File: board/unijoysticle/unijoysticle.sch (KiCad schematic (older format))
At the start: 12 parts, among them IC1 7405, IC2 7405, J1 DB9_Female, J2 DB9_Female, J3 Barrel_Jack, SW1 SW_Push

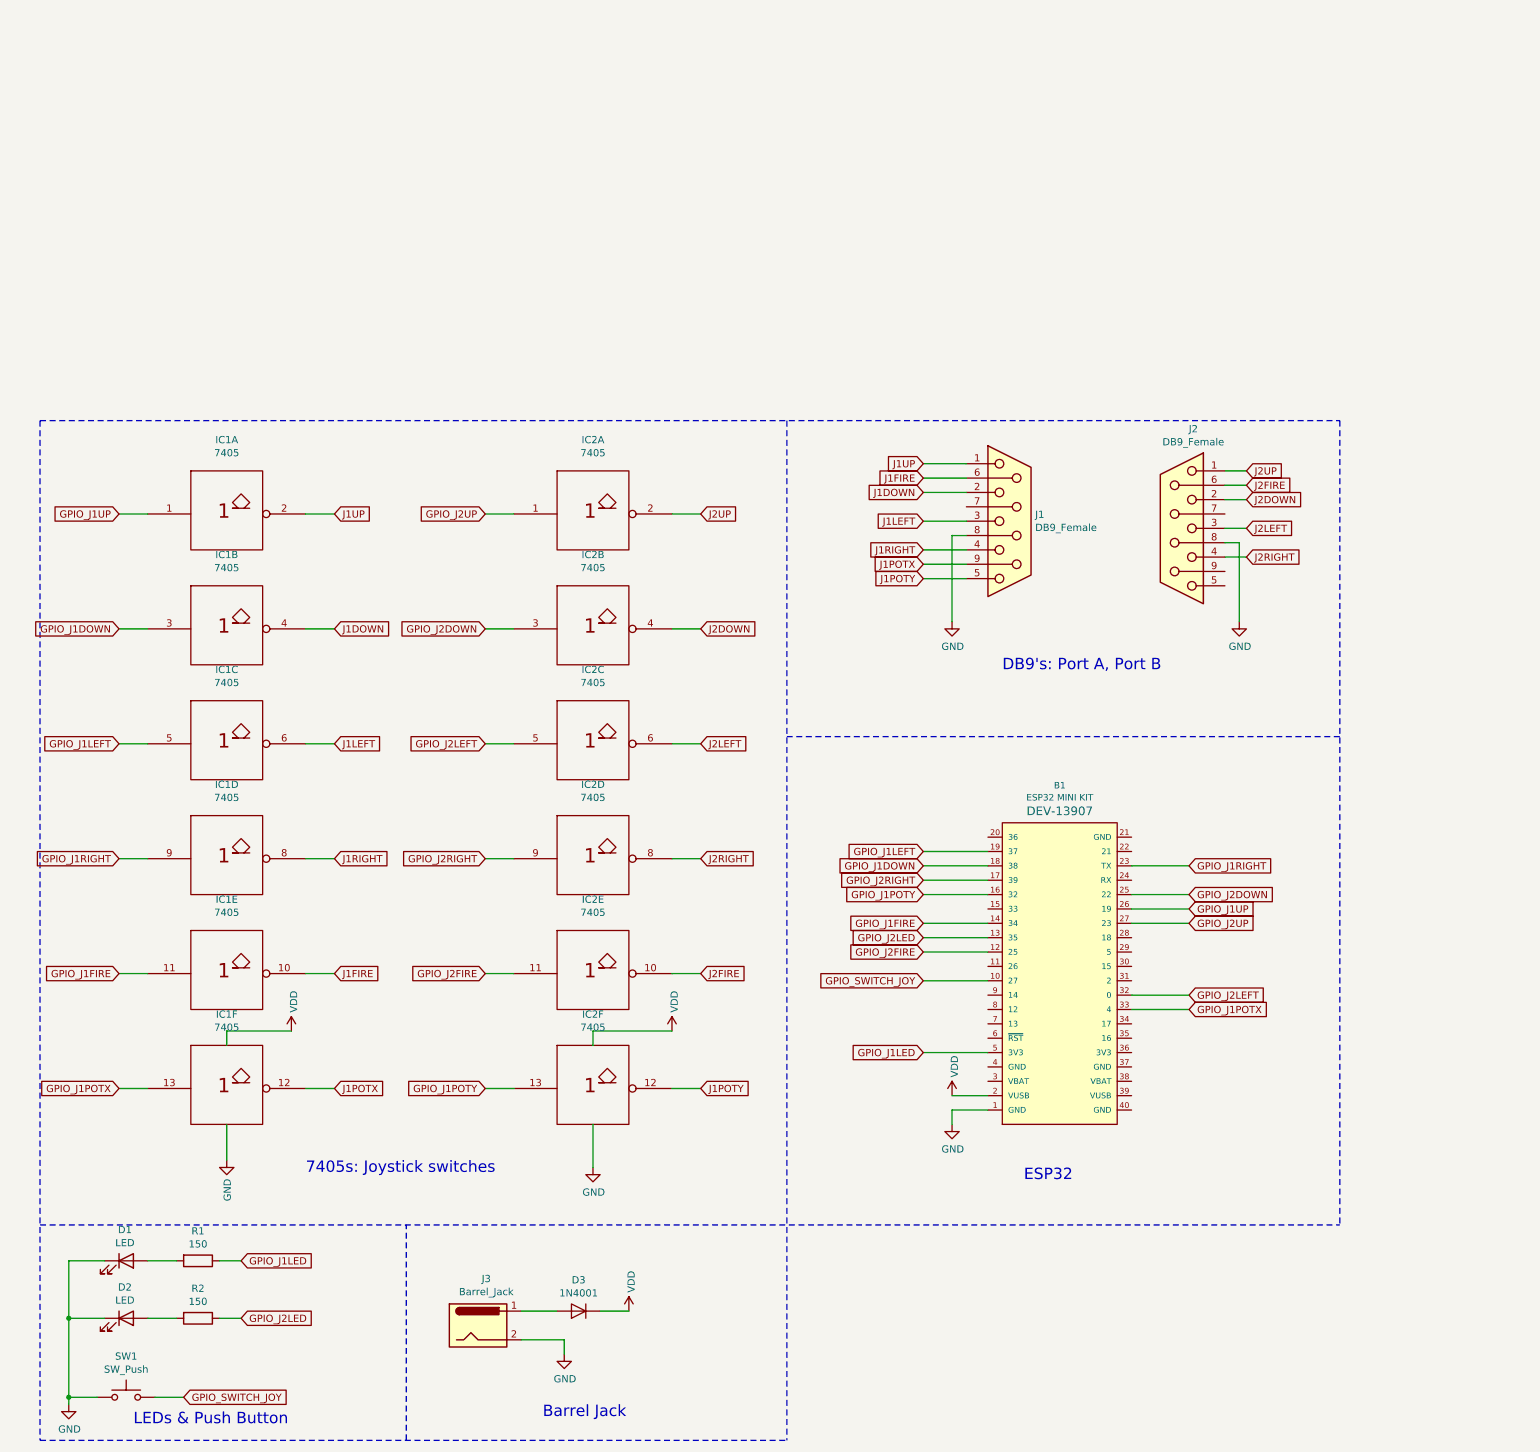
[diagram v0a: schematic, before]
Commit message: schematic: support for power from c64
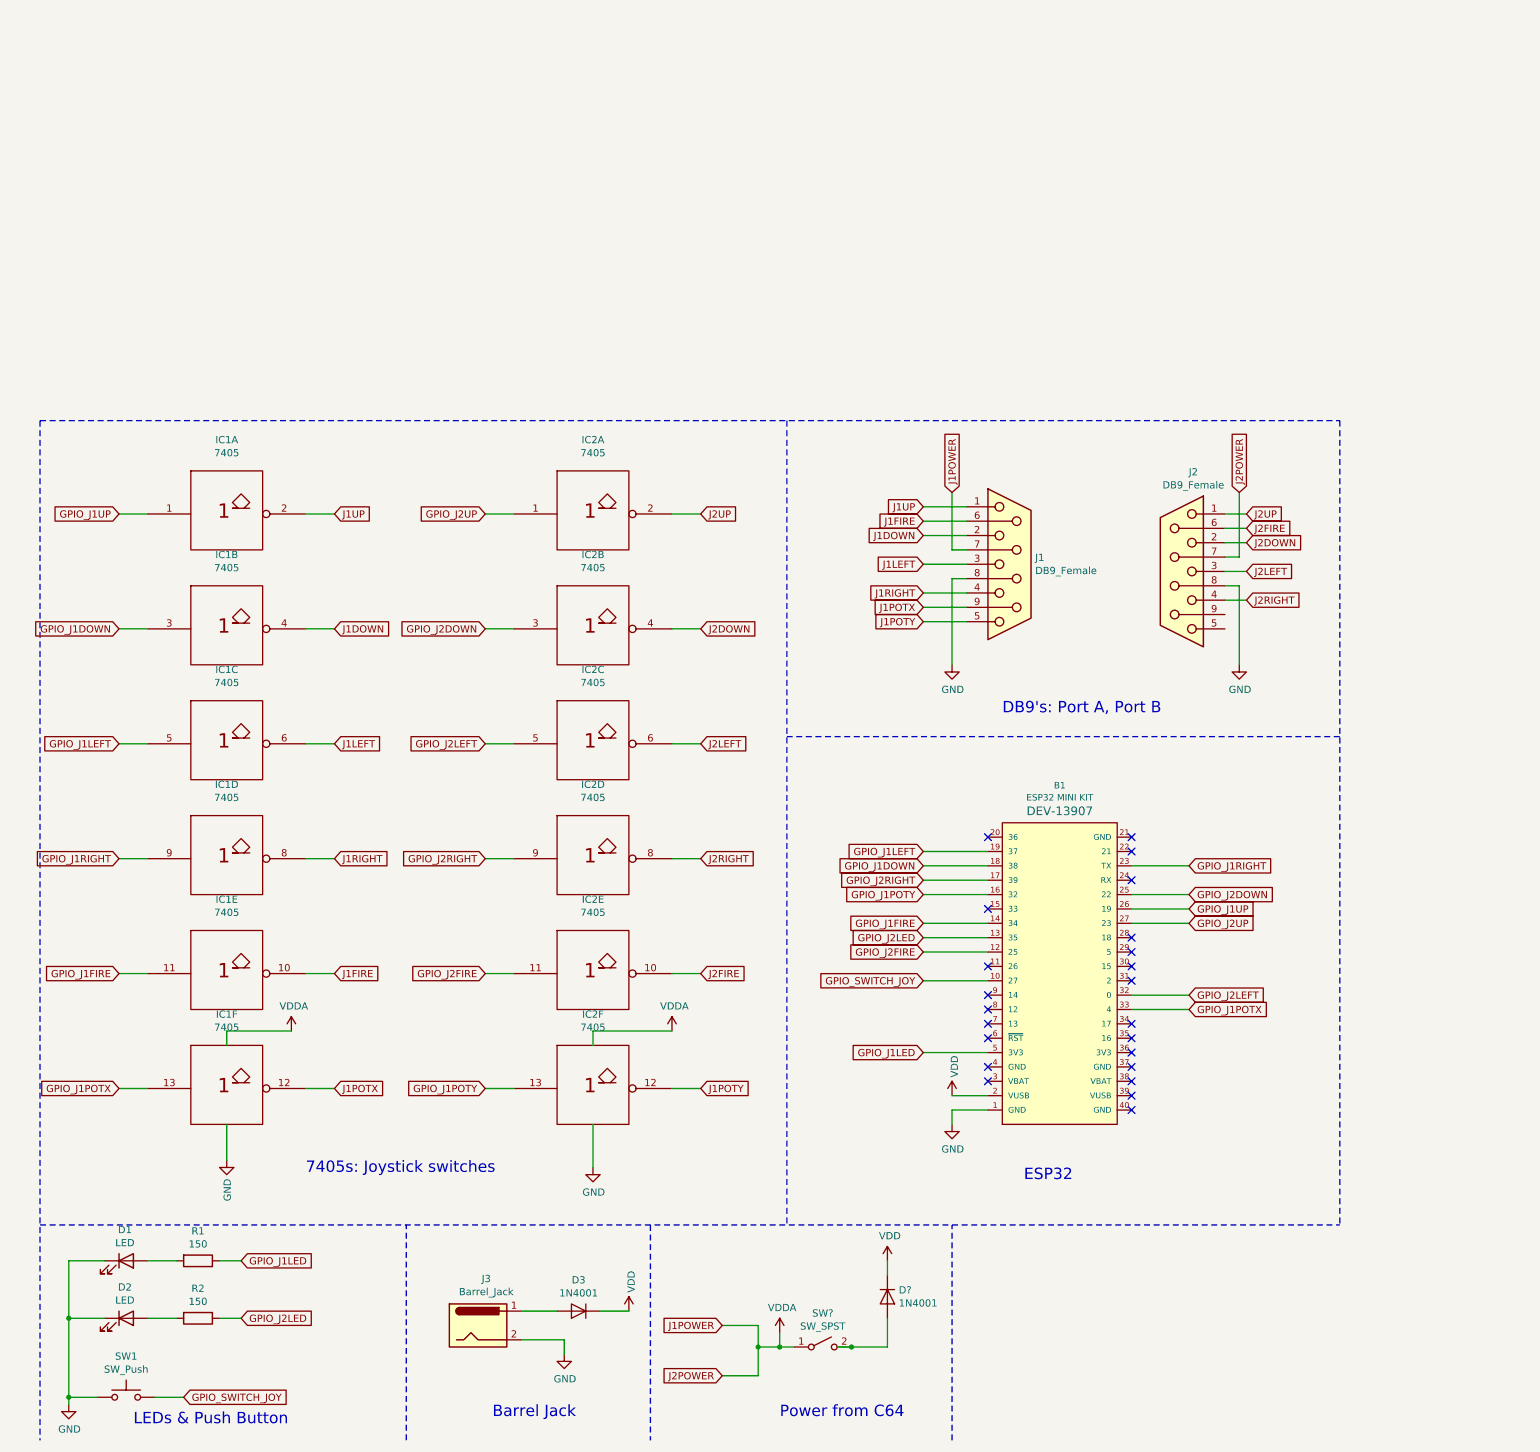
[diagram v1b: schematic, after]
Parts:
- added D?: 1N4001, Diode_THT:D_DO-41_SOD81_P10.16mm_Horizontal, symbol Diode:1N4001
- added SW?: SW_SPST, symbol Switch:SW_SPST
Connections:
- net VDD: now also D?.1 (K); no longer IC1.14 (Vcc), IC2.14 (Vcc)
- net VDDA: now reaches J1.7
- net VDDA: now also IC1.14 (Vcc), IC2.14 (Vcc), J2.7, SW?.1 (A)
- new net: D?.2 (A), SW?.2 (B)
- no-connect marks 0 -> 23
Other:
- note added: "Power from C64"
- moved on the sheet: J1, J2
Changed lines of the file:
@@
 EESchema Schematic File Version 4
 LIBS:unijoysticle-cache
-EELAYER 29 0
+EELAYER 30 0
 EELAYER END
 $Descr A4 11693 8268
@@
 Sheet 1 1
 Title "Unijoysticle 2"
-Date "2019-03-28"
-Rev "B"
+Date "2019-09-21"
+Rev "C"
 Comp "Retro Moe"
 Comment1 "Ricardo Quesada"
@@
 GPIO_J1POTY
 Wire Wire Line
-	7000 1000 6700 1000
-Wire Wire Line
-	7000 1100 6700 1100
-Wire Wire Line
-	7000 1200 6700 1200
+	7000 1300 6700 1300
 Wire Wire Line
 	7000 1400 6700 1400
 Wire Wire Line
-	7000 1600 6700 1600
+	7000 1500 6700 1500
 Wire Wire Line
 	7000 1700 6700 1700
 Wire Wire Line
-	7000 1800 6700 1800
-Text GLabel 6700 1000 0    50   Input ~ 0
+	7000 1900 6700 1900
+Wire Wire Line
+	7000 2000 6700 2000
+Wire Wire Line
+	7000 2100 6700 2100
+Text GLabel 6700 1300 0    50   Input ~ 0
 J1UP
-Text GLabel 6700 1200 0    50   Input ~ 0
+Text GLabel 6700 1500 0    50   Input ~ 0
 J1DOWN
+Text GLabel 6700 1700 0    50   Input ~ 0
+J1LEFT
 Text GLabel 6700 1400 0    50   Input ~ 0
-J1LEFT
-Text GLabel 6700 1100 0    50   Input ~ 0
 J1FIRE
-Text GLabel 6700 1800 0    50   Input ~ 0
+Text GLabel 6700 2100 0    50   Input ~ 0
 J1POTY
-Text GLabel 6700 1700 0    50   Input ~ 0
+Text GLabel 6700 2000 0    50   Input ~ 0
 J1POTX
-Text GLabel 6700 1600 0    50   Input ~ 0
+Text GLabel 6700 1900 0    50   Input ~ 0
 J1RIGHT
-Text GLabel 8950 1050 2    50   Input ~ 0
+Text GLabel 8950 1350 2    50   Input ~ 0
 J2UP
-Text GLabel 8950 1250 2    50   Input ~ 0
+Text GLabel 8950 1550 2    50   Input ~ 0
 J2DOWN
+Text GLabel 8950 1750 2    50   Input ~ 0
+J2LEFT
+Text GLabel 8950 1950 2    50   Input ~ 0
+J2RIGHT
 Text GLabel 8950 1450 2    50   Input ~ 0
-J2LEFT
-Text GLabel 8950 1650 2    50   Input ~ 0
-J2RIGHT
-Text GLabel 8950 1150 2    50   Input ~ 0
 J2FIRE
 Text GLabel 5150 1350 2    50   Input ~ 0
@@
 L Connector:DB9_Female J1
 U 1 1 5C705949
-P 7300 1400
-F 0 "J1" H 7479 1446 50  0000 L CNN
-F 1 "DB9_Female" H 7479 1355 50  0000 L CNN
-F 2 "Connector_Dsub:DSUB-9_Female_Horizontal_P2.77x2.84mm_EdgePinOffset9.40mm" H 7300 1400 50  0001 C CNN
-F 3 "" H 7300 1400 50  0001 C CNN
-	1    7300 1400
+P 7300 1700
+F 0 "J1" H 7479 1746 50  0000 L CNN
+F 1 "DB9_Female" H 7479 1655 50  0000 L CNN
+F 2 "Connector_Dsub:DSUB-9_Female_Horizontal_P2.77x2.84mm_EdgePinOffset9.40mm" H 7300 1700 50  0001 C CNN
+F 3 "" H 7300 1700 50  0001 C CNN
+	1    7300 1700
 	1    0    0    -1
 $EndComp
@@
 L Connector:DB9_Female J2
 U 1 1 5C705C0F
-P 8500 1450
-F 0 "J2" H 8420 2142 50  0000 C CNN
-F 1 "DB9_Female" H 8420 2051 50  0000 C CNN
-F 2 "Connector_Dsub:DSUB-9_Female_Horizontal_P2.77x2.84mm_EdgePinOffset9.40mm" H 8500 1450 50  0001 C CNN
-F 3 "" H 8500 1450 50  0001 C CNN
-	1    8500 1450
+P 8500 1750
+F 0 "J2" H 8420 2442 50  0000 C CNN
+F 1 "DB9_Female" H 8420 2351 50  0000 C CNN
+F 2 "Connector_Dsub:DSUB-9_Female_Horizontal_P2.77x2.84mm_EdgePinOffset9.40mm" H 8500 1750 50  0001 C CNN
+F 3 "" H 8500 1750 50  0001 C CNN
+	1    8500 1750
 	-1   0    0    -1
 $EndComp
 Wire Wire Line
-	8800 1050 8950 1050
-Wire Wire Line
-	8800 1150 8950 1150
-Wire Wire Line
-	8800 1250 8950 1250
-Wire Wire Line
-	8950 1450 8800 1450
-Wire Wire Line
-	8950 1650 8800 1650
+	8800 1350 8950 1350
+Wire Wire Line
+	8800 1450 8950 1450
+Wire Wire Line
+	8800 1550 8950 1550
+Wire Wire Line
+	8950 1750 8800 1750
+Wire Wire Line
+	8950 1950 8800 1950
 Wire Wire Line
 	8150 4200 8550 4200
@@
 Wire Wire Line
 	1100 5350 1300 5350
-$Comp
-L power:VDD #PWR0105
-U 1 1 5C862F14
-P 2300 4950
-F 0 "#PWR0105" H 2300 4800 50  0001 C CNN
-F 1 "VDD" V 2317 5078 50  0000 L CNN
-F 2 "" H 2300 4950 50  0001 C CNN
-F 3 "" H 2300 4950 50  0001 C CNN
-	1    2300 4950
-	1    0    0    -1
-$EndComp
 Wire Wire Line
 	2300 4950 1850 4950
@@
 Wire Wire Line
 	4400 4950 4950 4950
-$Comp
-L power:VDD #PWR0106
-U 1 1 5C86D74A
-P 4950 4950
-F 0 "#PWR0106" H 4950 4800 50  0001 C CNN
-F 1 "VDD" V 4967 5078 50  0000 L CNN
-F 2 "" H 4950 4950 50  0001 C CNN
-F 3 "" H 4950 4950 50  0001 C CNN
-	1    4950 4950
-	1    0    0    -1
-$EndComp
 $Comp
 L Device:LED D1
@@
 	1800 6950 1950 6950
 Wire Wire Line
-	8800 1550 8900 1550
-Wire Wire Line
-	8900 1550 8900 2100
-Wire Wire Line
-	7000 1500 6900 1500
-Wire Wire Line
-	6900 1500 6900 2100
+	8800 1850 8900 1850
+Wire Wire Line
+	8900 1850 8900 2400
+Wire Wire Line
+	7000 1800 6900 1800
+Wire Wire Line
+	6900 1800 6900 2400
 $Comp
 L power:GND #PWR0102
 U 1 1 5C8CE940
-P 6900 2100
-F 0 "#PWR0102" H 6900 1850 50  0001 C CNN
-F 1 "GND" H 6905 1927 50  0000 C CNN
-F 2 "" H 6900 2100 50  0001 C CNN
-F 3 "" H 6900 2100 50  0001 C CNN
-	1    6900 2100
+P 6900 2400
+F 0 "#PWR0102" H 6900 2150 50  0001 C CNN
+F 1 "GND" H 6905 2227 50  0000 C CNN
+F 2 "" H 6900 2400 50  0001 C CNN
+F 3 "" H 6900 2400 50  0001 C CNN
+	1    6900 2400
 	1    0    0    -1
 $EndComp
@@
 L power:GND #PWR0108
 U 1 1 5C8CEFE9
-P 8900 2100
-F 0 "#PWR0108" H 8900 1850 50  0001 C CNN
-F 1 "GND" H 8905 1927 50  0000 C CNN
-F 2 "" H 8900 2100 50  0001 C CNN
-F 3 "" H 8900 2100 50  0001 C CNN
-	1    8900 2100
+P 8900 2400
+F 0 "#PWR0108" H 8900 2150 50  0001 C CNN
+F 1 "GND" H 8905 2227 50  0000 C CNN
+F 2 "" H 8900 2400 50  0001 C CNN
+F 3 "" H 8900 2400 50  0001 C CNN
+	1    8900 2400
 	1    0    0    -1
 $EndComp
@@
 Wire Notes Line
 	550  700  9600 700
-Text Notes 7250 2450 0    79   ~ 0
+Text Notes 7250 2750 0    79   ~ 0
 DB9's: Port A, Port B
 Wire Notes Line
@@
 Text Notes 1200 7700 0    79   ~ 0
 LEDs & Push Button
-Wire Notes Line
-	5750 700  5750 7800
-Wire Notes Line
-	550  7800 5750 7800
-Text Notes 4050 7650 0    79   ~ 0
+Text Notes 3700 7650 0    79   ~ 0
 Barrel Jack
 $Comp
@@
 	1    0    0    -1
 $EndComp
+Wire Wire Line
+	8800 1650 8900 1650
+Wire Wire Line
+	8900 1650 8900 1200
+Wire Wire Line
+	7000 1600 6900 1600
+Wire Wire Line
+	6900 1600 6900 1200
+$Comp
+L power:VDDA #PWR?
+U 1 1 5D8CE89E
+P 2300 4950
+F 0 "#PWR?" H 2300 4800 50  0001 C CNN
+F 1 "VDDA" H 2317 5123 50  0000 C CNN
+F 2 "" H 2300 4950 50  0001 C CNN
+F 3 "" H 2300 4950 50  0001 C CNN
+	1    2300 4950
+	1    0    0    -1
+$EndComp
+$Comp
+L power:VDDA #PWR?
+U 1 1 5D8CF370
+P 4950 4950
+F 0 "#PWR?" H 4950 4800 50  0001 C CNN
+F 1 "VDDA" H 4967 5123 50  0000 C CNN
+F 2 "" H 4950 4950 50  0001 C CNN
+F 3 "" H 4950 4950 50  0001 C CNN
+	1    4950 4950
+	1    0    0    -1
+$EndComp
+Text GLabel 6900 1200 1    50   Input ~ 0
+J1POWER
+Text GLabel 8900 1200 1    50   Input ~ 0
+J2POWER
+NoConn ~ 8150 5500
+NoConn ~ 8150 5400
+NoConn ~ 8150 5300
+NoConn ~ 8150 5200
+NoConn ~ 8150 5100
+NoConn ~ 8150 5000
+NoConn ~ 8150 4900
+NoConn ~ 8150 4600
+NoConn ~ 8150 4500
+NoConn ~ 8150 4400
+NoConn ~ 8150 4300
+NoConn ~ 8150 3900
+NoConn ~ 8150 3700
+NoConn ~ 8150 3600
+NoConn ~ 7150 3600
+NoConn ~ 7150 4100
+NoConn ~ 7150 4500
+NoConn ~ 7150 4700
+NoConn ~ 7150 4800
+NoConn ~ 7150 4900
+NoConn ~ 7150 5000
+NoConn ~ 7150 5200
+NoConn ~ 7150 5300
+Text GLabel 5300 7000 0    50   Input ~ 0
+J1POWER
+Text GLabel 5300 7350 0    50   Input ~ 0
+J2POWER
+Wire Wire Line
+	5300 7000 5550 7000
+Wire Wire Line
+	5550 7350 5300 7350
+Wire Wire Line
+	6100 7150 6200 7150
+$Comp
+L power:VDD #PWR?
+U 1 1 5D9B72D2
+P 6450 6550
+F 0 "#PWR?" H 6450 6400 50  0001 C CNN
+F 1 "VDD" H 6467 6723 50  0000 C CNN
+F 2 "" H 6450 6550 50  0001 C CNN
+F 3 "" H 6450 6550 50  0001 C CNN
+	1    6450 6550
+	1    0    0    -1
+$EndComp
+$Comp
+L Switch:SW_SPST SW?
+U 1 1 5D9BBF38
+P 6000 7150
+F 0 "SW?" H 6000 7385 50  0000 C CNN
+F 1 "SW_SPST" H 6000 7294 50  0000 C CNN
+F 2 "" H 6000 7150 50  0001 C CNN
+F 3 "~" H 6000 7150 50  0001 C CNN
+	1    6000 7150
+	1    0    0    -1
+$EndComp
+Wire Wire Line
+	5550 7000 5550 7150
+Wire Wire Line
+	5550 7150 5700 7150
+Connection ~ 5550 7150
+Wire Wire Line
+	5550 7150 5550 7350
+Wire Wire Line
+	5700 7150 5700 7050
+$Comp
+L power:VDDA #PWR?
+U 1 1 5D9F1571
+P 5700 7050
+F 0 "#PWR?" H 5700 6900 50  0001 C CNN
+F 1 "VDDA" H 5717 7223 50  0000 C CNN
+F 2 "" H 5700 7050 50  0001 C CNN
+F 3 "" H 5700 7050 50  0001 C CNN
+	1    5700 7050
+	1    0    0    -1
+$EndComp
+Wire Wire Line
+	5800 7150 5700 7150
+Connection ~ 5700 7150
+Wire Wire Line
+	6200 7150 6450 7150
+Wire Wire Line
+	6450 7150 6450 6950
+Connection ~ 6200 7150
+$Comp
+L Diode:1N4001 D?
+U 1 1 5DA3B4FA
+P 6450 6800
+F 0 "D?" V 6404 6879 50  0000 L CNN
+F 1 "1N4001" V 6495 6879 50  0000 L CNN
+F 2 "Diode_THT:D_DO-41_SOD81_P10.16mm_Horizontal" H 6450 6625 50  0001 C CNN
+F 3 "http://www.vishay.com/docs/88503/1n4001.pdf" H 6450 6800 50  0001 C CNN
+	1    6450 6800
+	0    1    1    0
+$EndComp
+Wire Wire Line
+	6450 6650 6450 6550
+Wire Notes Line
+	4800 6300 4800 7800
+Wire Notes Line
+	5750 700  5750 6300
+Text Notes 5700 7650 0    79   ~ 0
+Power from C64
+Wire Notes Line
+	6900 7800 6900 6300
 $EndSCHEMATC

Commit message: layout: Rev C: Work in progress
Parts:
- D4: renamed from D?; footprint Diode_THT:D_DO-41_SOD81_P10.16mm_Horizontal -> Diode_THT:D_DO-41_SOD81_P7.62mm_Horizontal
- SW2: renamed from SW?; footprint (none) -> Button_Switch_THT:SW_DIP_SPSTx01_Slide_6.7x4.1mm_W7.62mm_P2.54mm_LowProfile
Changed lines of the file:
@@
 	6900 1600 6900 1200
 $Comp
-L power:VDDA #PWR?
+L power:VDDA #PWR0105
 U 1 1 5D8CE89E
 P 2300 4950
-F 0 "#PWR?" H 2300 4800 50  0001 C CNN
+F 0 "#PWR0105" H 2300 4800 50  0001 C CNN
 F 1 "VDDA" H 2317 5123 50  0000 C CNN
 F 2 "" H 2300 4950 50  0001 C CNN
@@
 $EndComp
 $Comp
-L power:VDDA #PWR?
+L power:VDDA #PWR0106
 U 1 1 5D8CF370
 P 4950 4950
-F 0 "#PWR?" H 4950 4800 50  0001 C CNN
+F 0 "#PWR0106" H 4950 4800 50  0001 C CNN
 F 1 "VDDA" H 4967 5123 50  0000 C CNN
 F 2 "" H 4950 4950 50  0001 C CNN
@@
 	6100 7150 6200 7150
 $Comp
-L power:VDD #PWR?
+L power:VDD #PWR0112
 U 1 1 5D9B72D2
 P 6450 6550
-F 0 "#PWR?" H 6450 6400 50  0001 C CNN
+F 0 "#PWR0112" H 6450 6400 50  0001 C CNN
 F 1 "VDD" H 6467 6723 50  0000 C CNN
 F 2 "" H 6450 6550 50  0001 C CNN
@@
 $EndComp
 $Comp
-L Switch:SW_SPST SW?
+L Switch:SW_SPST SW2
 U 1 1 5D9BBF38
 P 6000 7150
-F 0 "SW?" H 6000 7385 50  0000 C CNN
+F 0 "SW2" H 6000 7385 50  0000 C CNN
 F 1 "SW_SPST" H 6000 7294 50  0000 C CNN
-F 2 "" H 6000 7150 50  0001 C CNN
+F 2 "Button_Switch_THT:SW_DIP_SPSTx01_Slide_6.7x4.1mm_W7.62mm_P2.54mm_LowProfile" H 6000 7150 50  0001 C CNN
 F 3 "~" H 6000 7150 50  0001 C CNN
 	1    6000 7150
@@
 	5700 7150 5700 7050
 $Comp
-L power:VDDA #PWR?
+L power:VDDA #PWR0113
 U 1 1 5D9F1571
 P 5700 7050
-F 0 "#PWR?" H 5700 6900 50  0001 C CNN
+F 0 "#PWR0113" H 5700 6900 50  0001 C CNN
 F 1 "VDDA" H 5717 7223 50  0000 C CNN
 F 2 "" H 5700 7050 50  0001 C CNN
@@
 Connection ~ 6200 7150
 $Comp
-L Diode:1N4001 D?
+L Diode:1N4001 D4
 U 1 1 5DA3B4FA
 P 6450 6800
-F 0 "D?" V 6404 6879 50  0000 L CNN
+F 0 "D4" V 6404 6879 50  0000 L CNN
 F 1 "1N4001" V 6495 6879 50  0000 L CNN
-F 2 "Diode_THT:D_DO-41_SOD81_P10.16mm_Horizontal" H 6450 6625 50  0001 C CNN
+F 2 "Diode_THT:D_DO-41_SOD81_P7.62mm_Horizontal" H 6450 6625 50  0001 C CNN
 F 3 "http://www.vishay.com/docs/88503/1n4001.pdf" H 6450 6800 50  0001 C CNN
 	1    6450 6800
